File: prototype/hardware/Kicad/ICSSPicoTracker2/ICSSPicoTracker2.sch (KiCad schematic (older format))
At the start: 0 parts

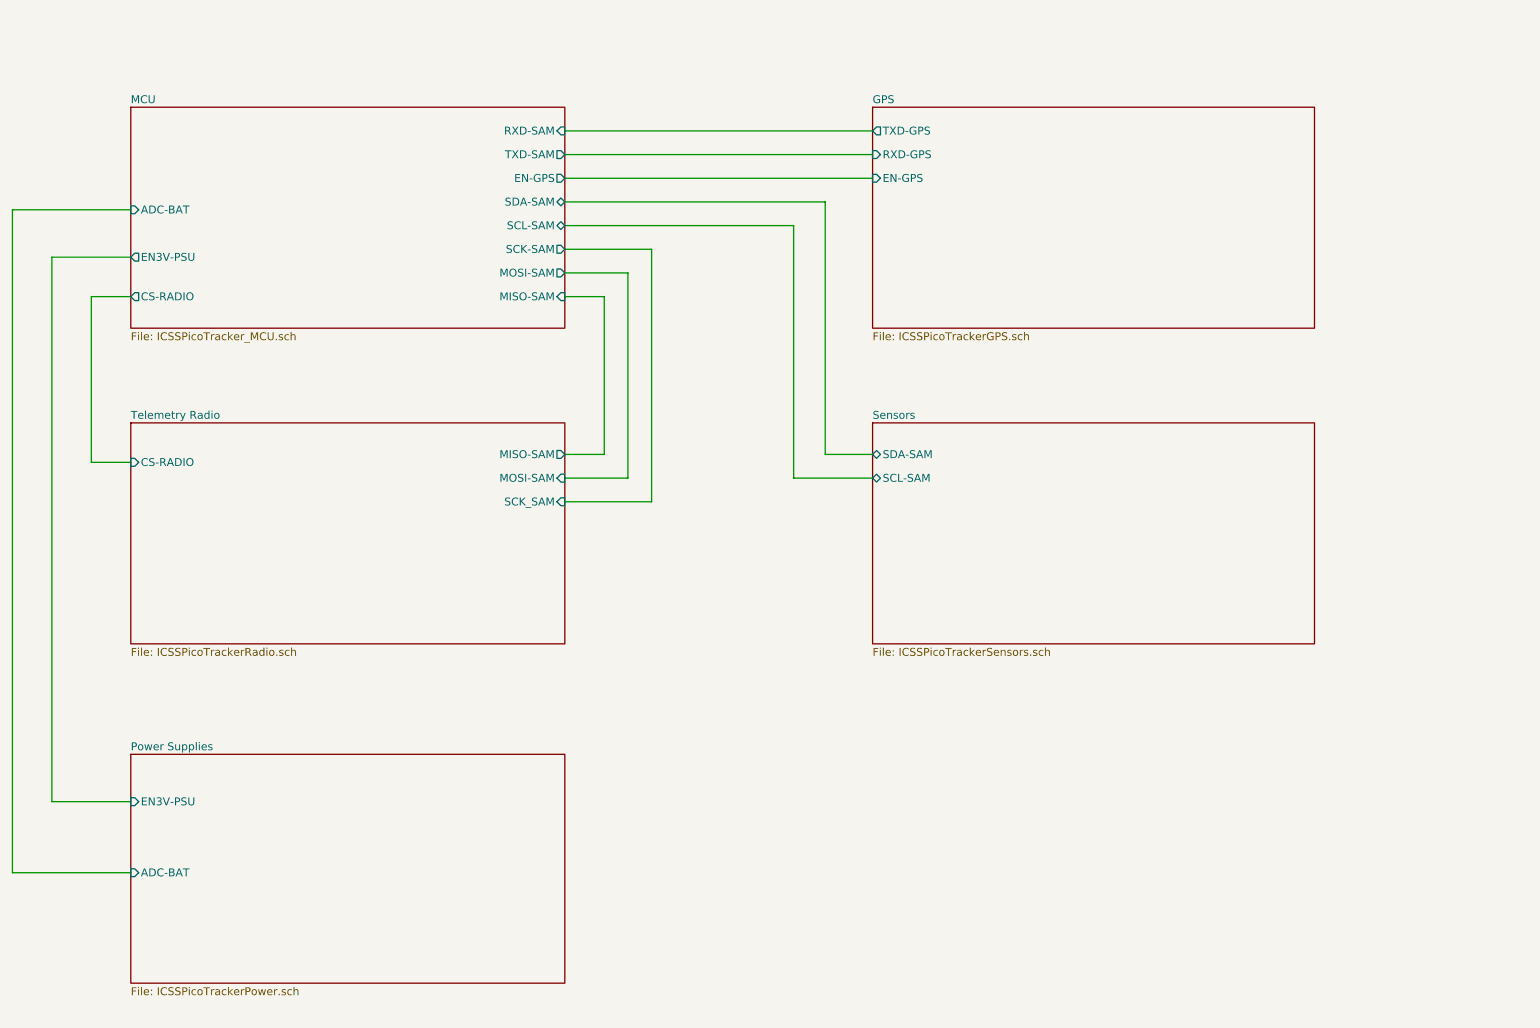
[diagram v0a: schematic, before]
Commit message: Updated Scehematics and Footprints
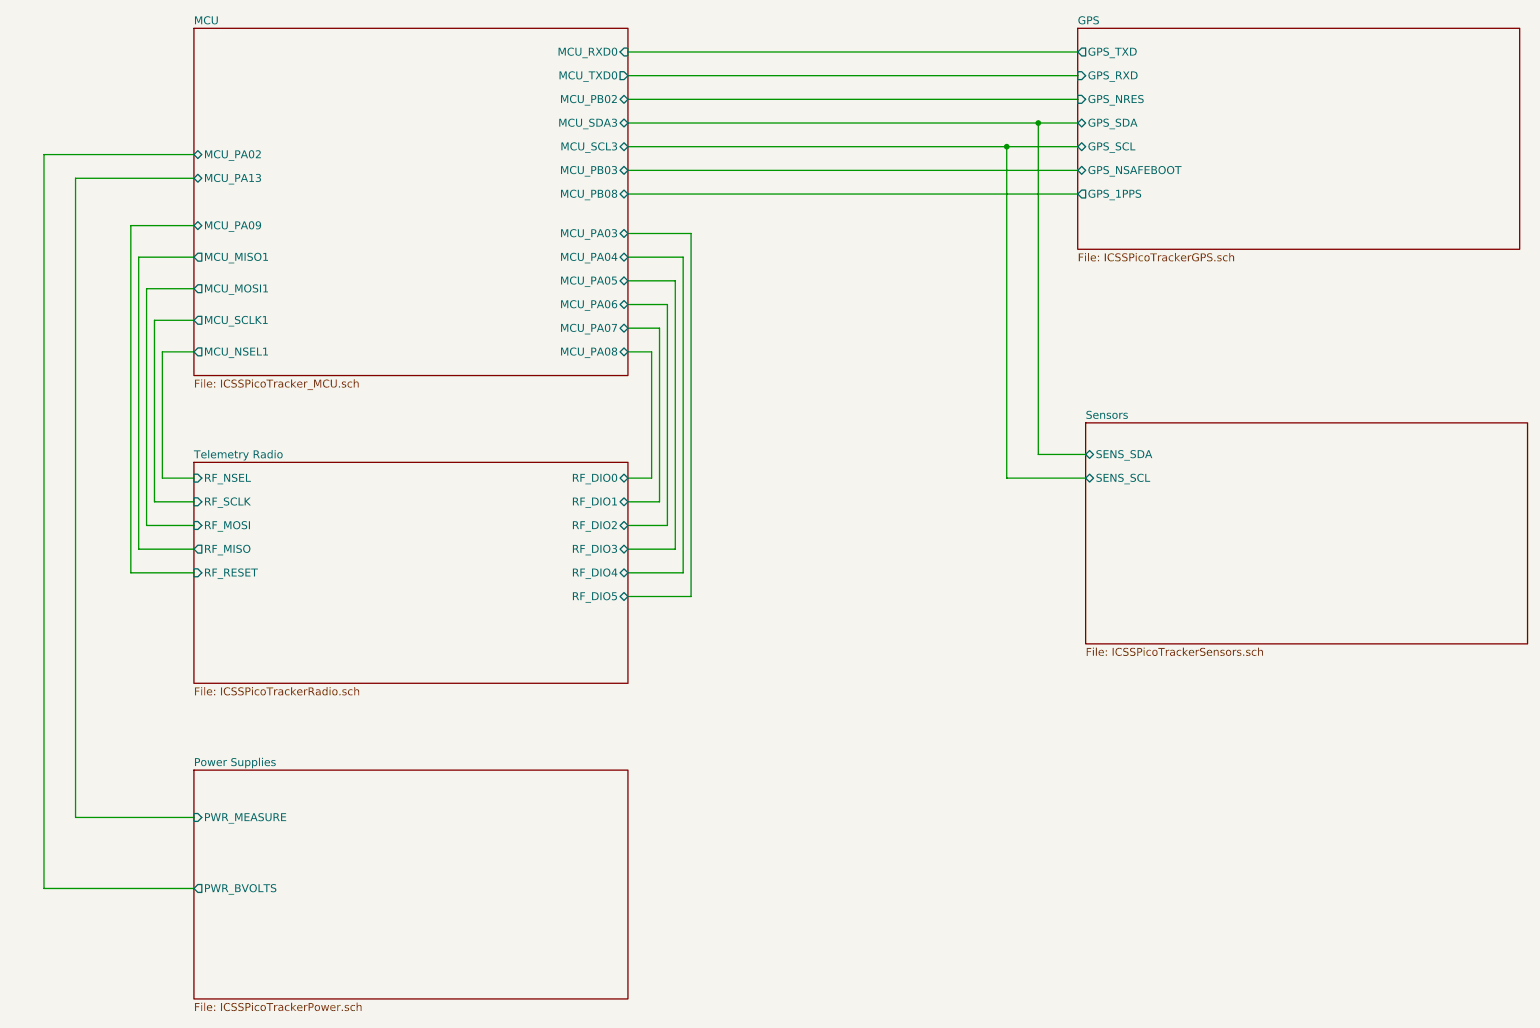
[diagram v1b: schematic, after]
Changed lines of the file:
@@
 $EndDescr
 $Sheet
-S 1650 1300 2750 1400
+S 2050 800  2750 2200
 U 5D288EB7
 F0 "MCU" 50
 F1 "ICSSPicoTracker_MCU.sch" 50
-F2 "RXD-SAM" I R 4400 1450 50
-F3 "TXD-SAM" O R 4400 1600 50
-F4 "SDA-SAM" B R 4400 1900 50
-F5 "SCL-SAM" B R 4400 2050 50
-F6 "SCK-SAM" O R 4400 2200 50
-F7 "MOSI-SAM" O R 4400 2350 50
-F8 "MISO-SAM" I R 4400 2500 50
-F9 "CS-RADIO" O L 1650 2500 50
-F10 "ADC-BAT" I L 1650 1950 50
-F11 "EN-GPS" O R 4400 1750 50
-F12 "EN3V-PSU" O L 1650 2250 50
+F2 "MCU_RXD0" I R 4800 950 50
+F3 "MCU_TXD0" O R 4800 1100 50
+F4 "MCU_SDA3" B R 4800 1400 50
+F5 "MCU_SCL3" B R 4800 1550 50
+F6 "MCU_PB02" B R 4800 1250 50
+F7 "MCU_PA08" B R 4800 2850 50
+F8 "MCU_PA07" B R 4800 2700 50
+F9 "MCU_PA06" B R 4800 2550 50
+F10 "MCU_PA05" B R 4800 2400 50
+F11 "MCU_PA04" B R 4800 2250 50
+F12 "MCU_PA03" B R 4800 2100 50
+F13 "MCU_NSEL1" O L 2050 2850 50
+F14 "MCU_SCLK1" O L 2050 2650 50
+F15 "MCU_MOSI1" O L 2050 2450 50
+F16 "MCU_MISO1" O L 2050 2250 50
+F17 "MCU_PA09" B L 2050 2050 50
+F18 "MCU_PB03" B R 4800 1700 50
+F19 "MCU_PB08" B R 4800 1850 50
+F20 "MCU_PA02" B L 2050 1600 50
+F21 "MCU_PA13" B L 2050 1750 50
 $EndSheet
 $Sheet
-S 1650 3300 2750 1400
+S 2050 3550 2750 1400
 U 5D2ABA40
 F0 "Telemetry Radio" 50
 F1 "ICSSPicoTrackerRadio.sch" 50
-F2 "CS-RADIO" I L 1650 3550 50
-F3 "MISO-SAM" O R 4400 3500 50
-F4 "MOSI-SAM" I R 4400 3650 50
-F5 "SCK_SAM" I R 4400 3800 50
+F2 "RF_SCLK" I L 2050 3800 50
+F3 "RF_NSEL" I L 2050 3650 50
+F4 "RF_MOSI" I L 2050 3950 50
+F5 "RF_MISO" O L 2050 4100 50
+F6 "RF_RESET" I L 2050 4250 50
+F7 "RF_DIO0" B R 4800 3650 50
+F8 "RF_DIO1" B R 4800 3800 50
+F9 "RF_DIO2" B R 4800 3950 50
+F10 "RF_DIO3" B R 4800 4100 50
+F11 "RF_DIO4" B R 4800 4250 50
+F12 "RF_DIO5" B R 4800 4400 50
 $EndSheet
 $Sheet
-S 1650 5400 2750 1450
+S 2050 5500 2750 1450
 U 5D2ABCEA
 F0 "Power Supplies" 50
 F1 "ICSSPicoTrackerPower.sch" 50
-F2 "ADC-BAT" I L 1650 6150 50
-F3 "EN3V-PSU" I L 1650 5700 50
+F2 "PWR_BVOLTS" O L 2050 6250 50
+F3 "PWR_MEASURE" I L 2050 5800 50
 $EndSheet
 $Sheet
-S 6350 1300 2800 1400
+S 7650 800  2800 1400
 U 5D2ABE03
 F0 "GPS" 50
 F1 "ICSSPicoTrackerGPS.sch" 50
-F2 "TXD-GPS" O L 6350 1450 50
-F3 "RXD-GPS" I L 6350 1600 50
-F4 "EN-GPS" I L 6350 1750 50
+F2 "GPS_TXD" O L 7650 950 50
+F3 "GPS_RXD" I L 7650 1100 50
+F4 "GPS_NRES" I L 7650 1250 50
+F5 "GPS_SDA" B L 7650 1400 50
+F6 "GPS_SCL" B L 7650 1550 50
+F7 "GPS_NSAFEBOOT" B L 7650 1700 50
+F8 "GPS_1PPS" O L 7650 1850 50
 $EndSheet
 $Sheet
-S 6350 3300 2800 1400
+S 7700 3300 2800 1400
 U 5D2ABE8A
 F0 "Sensors" 50
 F1 "ICSSPicoTrackerSensors.sch" 50
-F2 "SDA-SAM" B L 6350 3500 50
-F3 "SCL-SAM" B L 6350 3650 50
+F2 "SENS_SDA" B L 7700 3500 50
+F3 "SENS_SCL" B L 7700 3650 50
 $EndSheet
 Wire Wire Line
-	1650 2500 1400 2500
+	7400 3500 7700 3500
 Wire Wire Line
-	1400 2500 1400 3550
+	7200 3650 7700 3650
 Wire Wire Line
-	1400 3550 1650 3550
+	4800 2850 4950 2850
 Wire Wire Line
-	4400 2500 4650 2500
+	4950 2850 4950 3650
 Wire Wire Line
-	4650 3500 4400 3500
+	4950 3650 4800 3650
 Wire Wire Line
-	4800 2350 4800 3650
+	4800 2700 5000 2700
 Wire Wire Line
-	4800 3650 4400 3650
+	5000 2700 5000 3800
 Wire Wire Line
-	4400 2200 4950 2200
+	5000 3800 4800 3800
 Wire Wire Line
-	4950 2200 4950 3800
+	4800 2550 5050 2550
 Wire Wire Line
-	4400 1450 6350 1450
+	5050 2550 5050 3950
 Wire Wire Line
-	4400 1600 6350 1600
+	5050 3950 4800 3950
 Wire Wire Line
-	4400 1900 6050 1900
+	4800 2400 5100 2400
 Wire Wire Line
-	6050 1900 6050 3500
+	5100 2400 5100 4100
 Wire Wire Line
-	6050 3500 6350 3500
+	5100 4100 4800 4100
 Wire Wire Line
-	4400 2050 5850 2050
+	4800 2250 5150 2250
 Wire Wire Line
-	5850 2050 5850 3650
+	5150 2250 5150 4250
 Wire Wire Line
-	4650 2500 4650 3500
+	5150 4250 4800 4250
 Wire Wire Line
-	4400 2350 4800 2350
+	4800 2100 5200 2100
 Wire Wire Line
-	4400 3800 4950 3800
+	5200 2100 5200 4400
 Wire Wire Line
-	5850 3650 6350 3650
+	5200 4400 4800 4400
 Wire Wire Line
-	4400 1750 6350 1750
+	4800 950  7650 950
 Wire Wire Line
-	900  1950 1650 1950
+	4800 1100 7650 1100
 Wire Wire Line
-	900  6150 1650 6150
+	4800 1400 7400 1400
 Wire Wire Line
-	900  1950 900  6150
+	4800 1550 7200 1550
 Wire Wire Line
-	1150 2250 1150 5700
+	4800 1250 7650 1250
 Wire Wire Line
-	1150 5700 1650 5700
+	7400 3500 7400 1400
+Connection ~ 7400 1400
 Wire Wire Line
-	1150 2250 1650 2250
+	7400 1400 7650 1400
+Wire Wire Line
+	7200 3650 7200 1550
+Connection ~ 7200 1550
+Wire Wire Line
+	7200 1550 7650 1550
+Wire Wire Line
+	4800 1700 7650 1700
+Wire Wire Line
+	7650 1850 4800 1850
+Wire Wire Line
+	2050 3650 1850 3650
+Wire Wire Line
+	1850 3650 1850 2850
+Wire Wire Line
+	1850 2850 2050 2850
+Wire Wire Line
+	2050 2650 1800 2650
+Wire Wire Line
+	1800 2650 1800 3800
+Wire Wire Line
+	1800 3800 2050 3800
+Wire Wire Line
+	2050 3950 1750 3950
+Wire Wire Line
+	1750 3950 1750 2450
+Wire Wire Line
+	1750 2450 2050 2450
+Wire Wire Line
+	2050 2250 1700 2250
+Wire Wire Line
+	1700 2250 1700 4100
+Wire Wire Line
+	1700 4100 2050 4100
+Wire Wire Line
+	2050 4250 1650 4250
+Wire Wire Line
+	1650 4250 1650 2050
+Wire Wire Line
+	1650 2050 2050 2050
+Wire Wire Line
+	2050 5800 1300 5800
+Wire Wire Line
+	1300 5800 1300 1750
+Wire Wire Line
+	1300 1750 2050 1750
+Wire Wire Line
+	2050 1600 1100 1600
+Wire Wire Line
+	1100 1600 1100 6250
+Wire Wire Line
+	1100 6250 2050 6250
 $EndSCHEMATC
